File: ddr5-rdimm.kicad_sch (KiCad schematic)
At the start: 31 parts, among them J2 Bus_DDR5_DDR504111002KQ, Q10 BSS138PW, Q11 BSS138PW, Q9 BSS138PW, SW3 SW_KMR211NGLFS_SMD

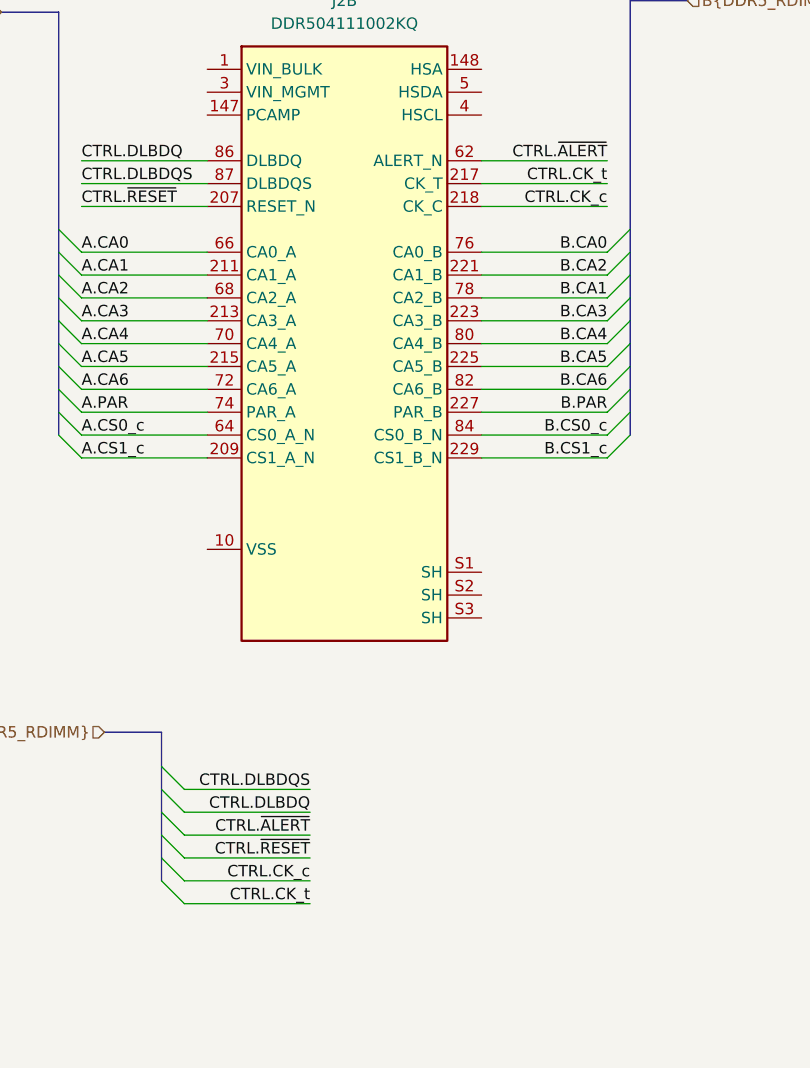
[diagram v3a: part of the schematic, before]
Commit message: [#66521] Add Layout for A.CA[0..7], B.CA[0..7]
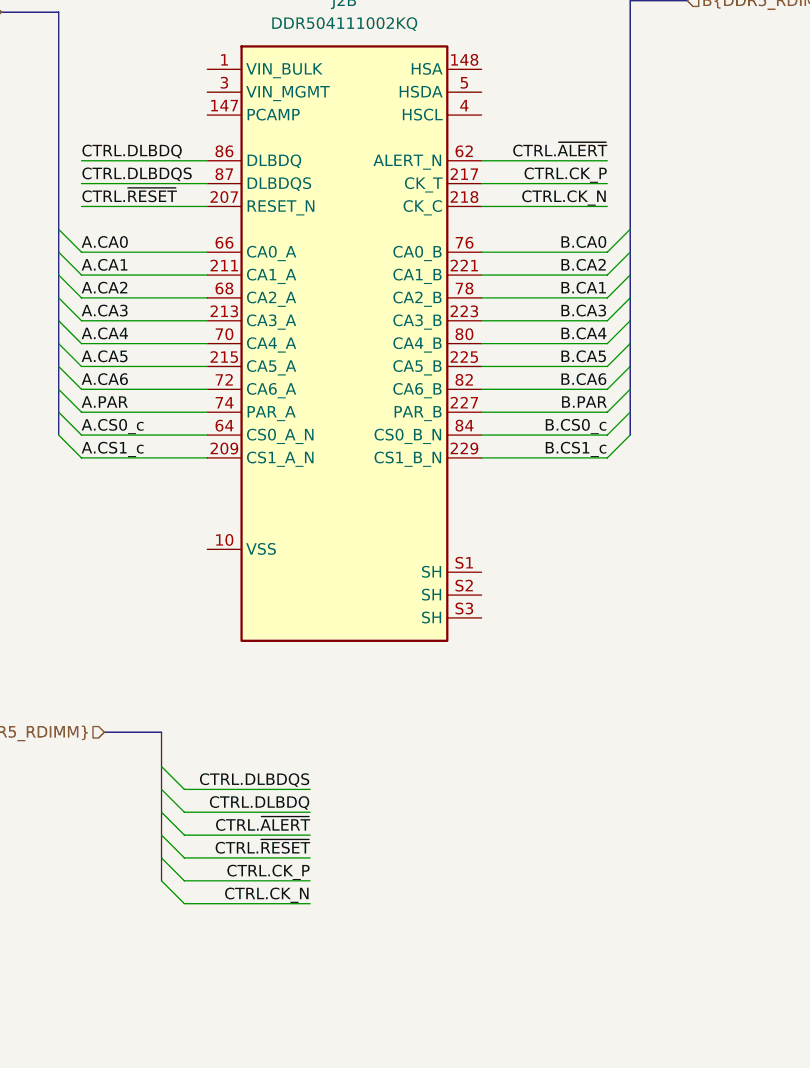
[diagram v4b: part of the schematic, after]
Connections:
- net CTRL.CK_c renamed CTRL.CK_N
- net CTRL.CK_t renamed CTRL.CK_P
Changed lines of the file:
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@@
     (effects (font (size 1.27 1.27)) (justify right bottom))
   )
-  (label "CTRL.CK_t" (at 214.63 62.23 180) (fields_autoplaced)
+  (label "CTRL.CK_P" (at 214.63 62.23 180) (fields_autoplaced)
     (effects (font (size 1.27 1.27)) (justify right bottom))
   )
@@
     (effects (font (size 1.27 1.27)) (justify right bottom))
   )
-  (label "CTRL.CK_c" (at 181.61 139.7 180) (fields_autoplaced)
+  (label "CTRL.CK_P" (at 181.61 139.7 180) (fields_autoplaced)
     (effects (font (size 1.27 1.27)) (justify right bottom))
   )
@@
     (effects (font (size 1.27 1.27)) (justify left bottom))
   )
-  (label "CTRL.CK_c" (at 214.63 64.77 180) (fields_autoplaced)
+  (label "CTRL.CK_N" (at 214.63 64.77 180) (fields_autoplaced)
     (effects (font (size 1.27 1.27)) (justify right bottom))
   )
@@
     (effects (font (size 1.27 1.27)) (justify right bottom))
   )
-  (label "CTRL.CK_t" (at 181.61 142.24 180) (fields_autoplaced)
-    (effects (font (size 1.27 1.27)) (justify right bottom))
-  )
+  (label "CTRL.CK_N" (at 181.61 142.24 180) (fields_autoplaced)
+    (effects (font (size 1.27 1.27)) (justify right bottom))
+  )

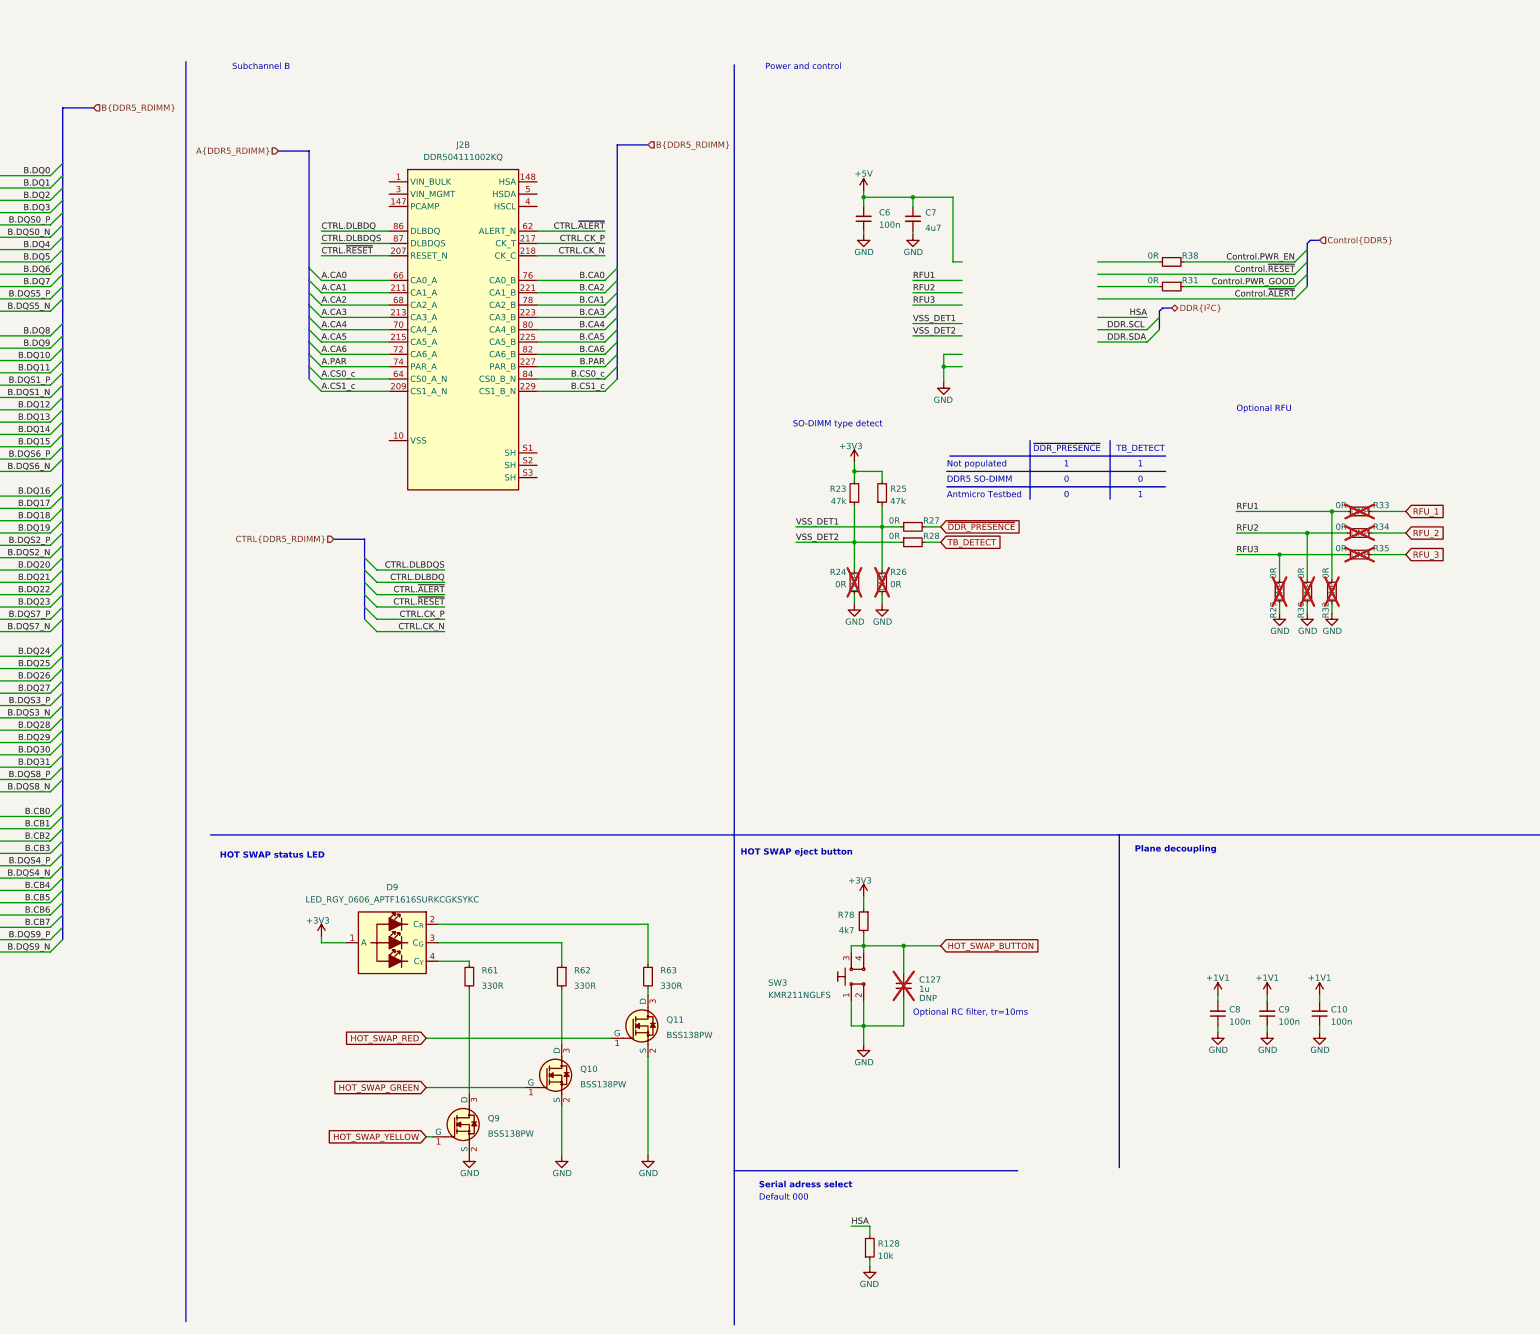
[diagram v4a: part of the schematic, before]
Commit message: [#66521] Cleanup DDR5 sheet
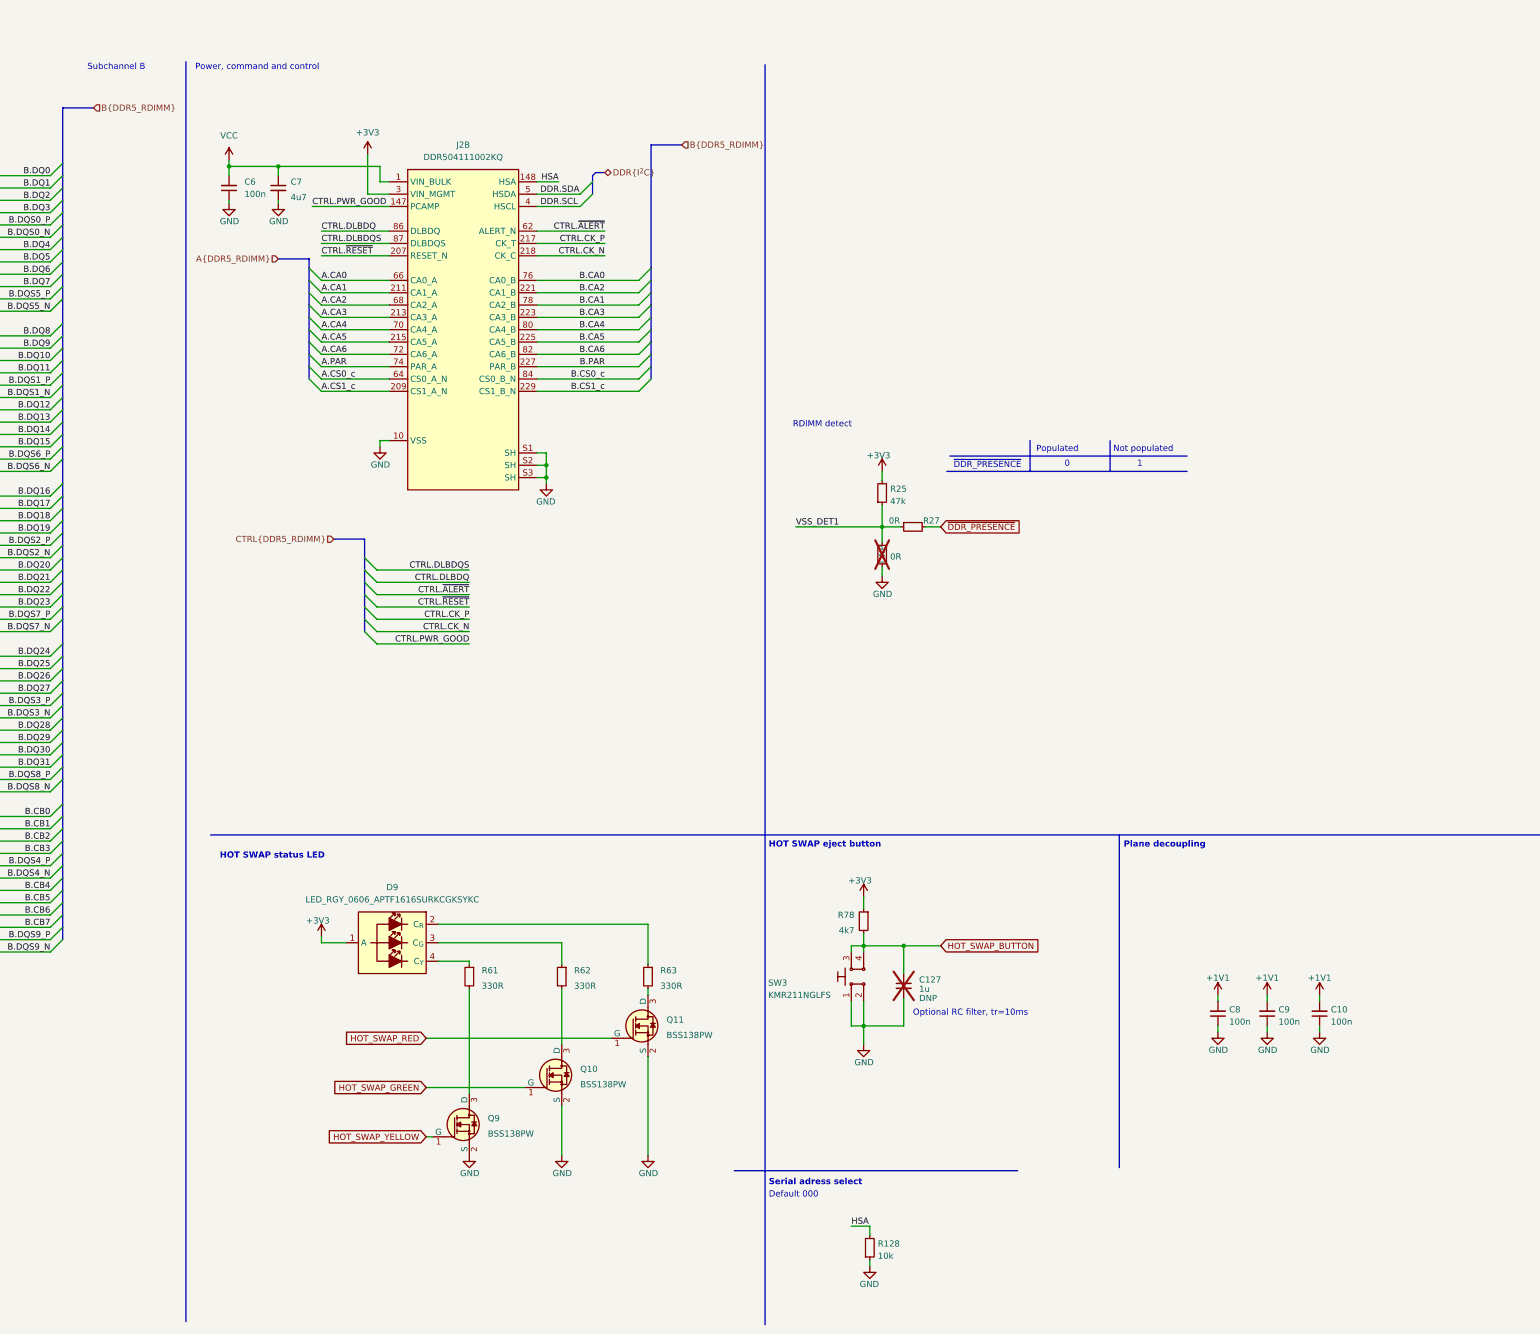
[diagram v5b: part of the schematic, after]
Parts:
- removed R23: R_47k_0402, antmicro-footprints:R_0402_1005Metric, symbol antmicroResistors0402:R_47k_0402
- removed R24, R28, R29, R30, R31, R32, R33, R34, R35, R38: R_0R_0402, antmicro-footprints:R_0402_1005Metric, symbol antmicroResistors0402:R_0R_0402
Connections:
- net +5V is gone; now on net VCC: C6.2, C7.1
- net +3V3: now also J2.3 (VIN_MGMT)
- net DDR.SCL: now also J2.4 (HSCL)
- net DDR.SDA: now also J2.5 (HSDA)
- net GND: now also J2.10 (VSS), J2.101 (VSS), J2.103 (VSS), J2.106 (VSS), J2.108 (VSS), J2.110 (VSS), J2.112 (VSS), J2.114 (VSS), J2.117 (VSS), J2.119 (VSS), J2.121 (VSS), J2.123 (VSS), J2.125 (VSS), J2.128 (VSS), J2.13 (VSS), J2.130 (VSS), J2.132 (VSS), J2.134 (VSS), J2.136 (VSS), J2.139 (VSS), J2.141 (VSS), J2.143 (VSS), J2.15 (VSS), J2.151 (VSS), J2.153 (VSS), J2.155 (VSS), J2.158 (VSS), J2.160 (VSS), J2.162 (VSS), J2.164 (VSS), J2.166 (VSS), J2.169 (VSS), J2.17 (VSS), J2.171 (VSS), J2.173 (VSS), J2.175 (VSS), J2.177 (VSS), J2.180 (VSS), J2.182 (VSS), J2.184 (VSS), J2.186 (VSS), J2.188 (VSS), J2.19 (VSS), J2.191 (VSS), J2.193 (VSS), J2.195 (VSS), J2.197 (VSS), J2.199 (VSS), J2.202 (VSS), J2.204 (VSS), J2.206 (VSS), J2.208 (VSS), J2.21 (VSS), J2.210 (VSS), J2.212 (VSS), J2.214 (VSS), J2.216 (VSS), J2.219 (VSS), J2.222 (VSS), J2.224 (VSS), J2.226 (VSS), J2.228 (VSS), J2.230 (VSS), J2.233 (VSS), J2.235 (VSS), J2.237 (VSS), J2.24 (VSS), J2.240 (VSS), J2.242 (VSS), J2.244 (VSS), J2.246 (VSS), J2.248 (VSS), J2.251 (VSS), J2.253 (VSS), J2.255 (VSS), J2.257 (VSS), J2.259 (VSS), J2.26 (VSS), J2.262 (VSS), J2.264 (VSS), J2.266 (VSS), J2.268 (VSS), J2.270 (VSS), J2.273 (VSS), J2.275 (VSS), J2.277 (VSS), J2.279 (VSS), J2.28 (VSS), J2.281 (VSS), J2.284 (VSS), J2.286 (VSS), J2.288 (VSS), J2.30 (VSS), J2.32 (VSS), J2.35 (VSS), J2.37 (VSS), J2.39 (VSS), J2.41 (VSS), J2.43 (VSS), J2.46 (VSS), J2.48 (VSS), J2.50 (VSS), J2.52 (VSS), J2.54 (VSS), J2.57 (VSS), J2.59 (VSS), J2.6 (VSS), J2.61 (VSS), J2.63 (VSS), J2.65 (VSS), J2.67 (VSS), J2.69 (VSS), J2.71 (VSS), J2.73 (VSS), J2.75 (VSS), J2.77 (VSS), J2.79 (VSS), J2.8 (VSS), J2.81 (VSS), J2.83 (VSS), J2.85 (VSS), J2.88 (VSS), J2.90 (VSS), J2.92 (VSS), J2.95 (VSS), J2.97 (VSS), J2.99 (VSS), J2.S1 (SH), J2.S2 (SH), J2.S3 (SH)
- net HSA: now also J2.148 (HSA)
- net VCC: now reaches J2.1 (VIN_BULK), J2.145 (VIN_BULK), J2.146 (VIN_BULK)
- net CTRL.PWR_GOOD: now reaches J2.147 (PCAMP)
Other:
- note added: "Populated"
- note added: "Power, command and control"
- note added: "RDIMM detect"
- note removed: "Antmicro Testbed"
- note removed: "DDR5 SO-DIMM"
- note removed: "Optional RFU"
- note removed: "Power and control"
- note removed: "SO-DIMM type detect"
- note removed: "TB_DETECT"
- moved on the sheet: C6, C7
